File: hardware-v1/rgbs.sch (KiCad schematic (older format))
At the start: 10 parts, among them U15 NMEA_RGB, U2 SN74HCT245, U4 N2K_RGB, U5 WIFI_RGB

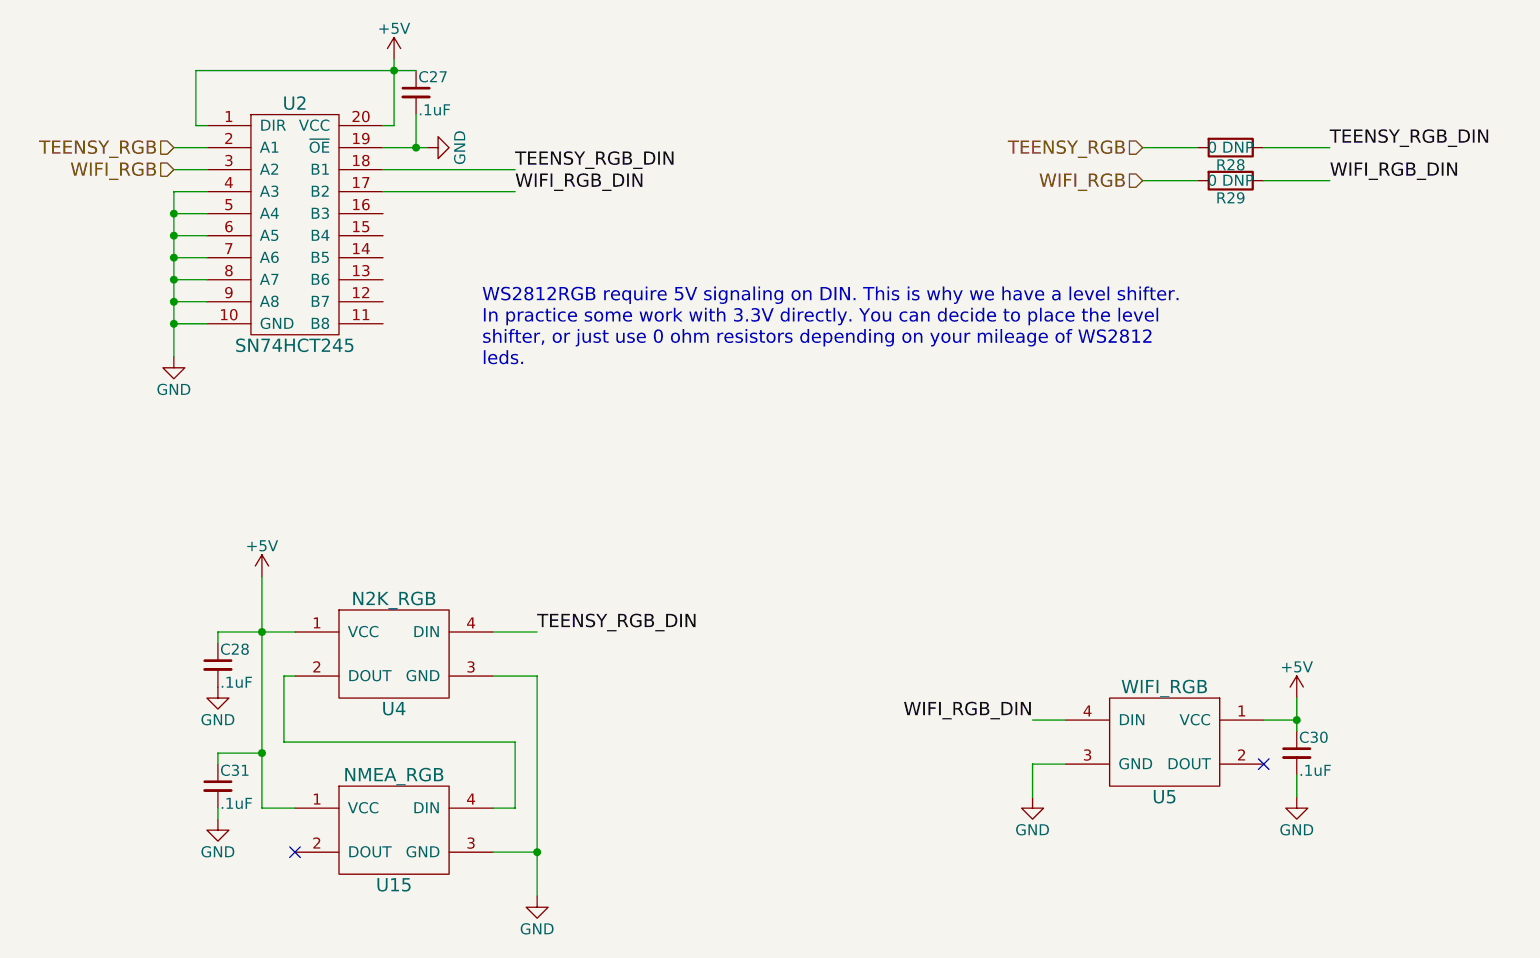
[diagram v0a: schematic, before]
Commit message: First draft of revision B
Lots of changes to the board. Almost completely re-layed out.

Will do some verification now.
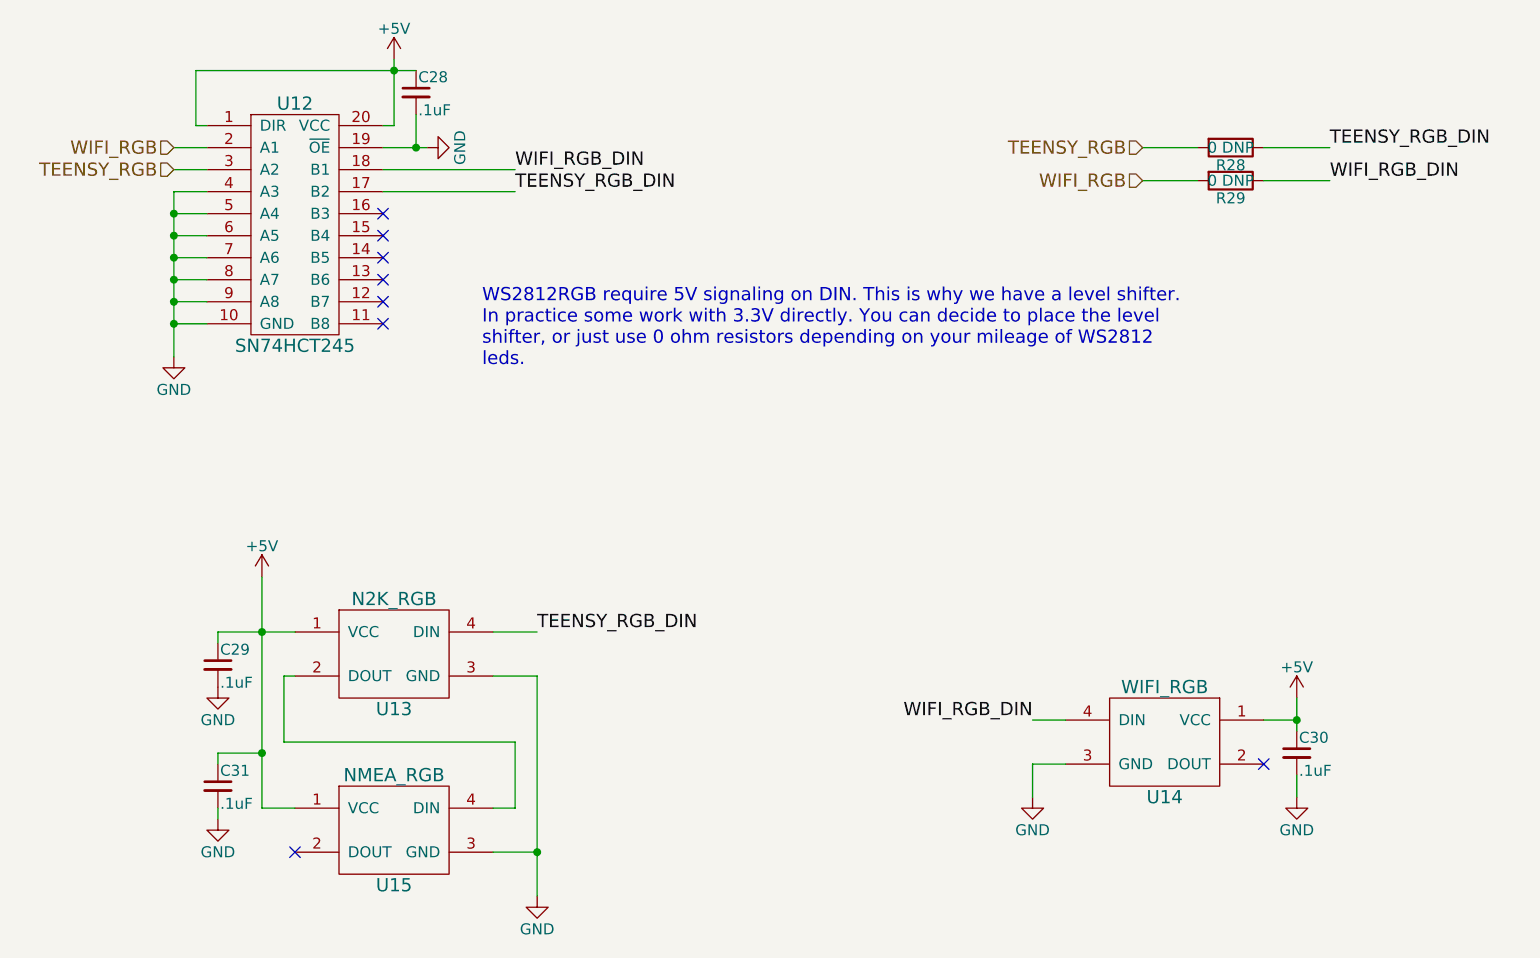
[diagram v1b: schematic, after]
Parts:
- renumbered C27 to C28, C28 to C29, U2 to U12, U4 to U13, U5 to U14
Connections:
- net TEENSY_RGB: now also U12.3 (A2); no longer U12.2 (A1)
- net TEENSY_RGB_DIN: now also U12.17 (B2); no longer U12.18 (B1)
- net WIFI_RGB: now also U12.2 (A1); no longer U12.3 (A2)
- net WIFI_RGB_DIN: now also U12.18 (B1); no longer U12.17 (B2)
- no-connect marks 2 -> 8
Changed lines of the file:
@@
 $EndDescr
 $Comp
-L WS2812RGB U4
+L WS2812RGB U13
 U 1 1 56A15737
 P 3750 4000
-F 0 "U4" H 3750 3750 60  0000 C CNN
+F 0 "U13" H 3750 3750 60  0000 C CNN
 F 1 "N2K_RGB" H 3750 4250 60  0000 C CNN
 F 2 "bb:WS2818RGB" H 3750 4050 60  0001 C CNN
@@
 $EndComp
 $Comp
-L GND #PWR073
+L GND #PWR074
 U 1 1 56A1574F
 P 4400 5100
-F 0 "#PWR073" H 4400 4850 50  0001 C CNN
+F 0 "#PWR074" H 4400 4850 50  0001 C CNN
 F 1 "GND" H 4400 4950 50  0000 C CNN
 F 2 "" H 4400 5100 60  0000 C CNN
@@
 $EndComp
 $Comp
-L +5V #PWR074
+L +5V #PWR075
 U 1 1 56A15759
 P 3150 3650
-F 0 "#PWR074" H 3150 3500 50  0001 C CNN
+F 0 "#PWR075" H 3150 3500 50  0001 C CNN
 F 1 "+5V" H 3150 3790 50  0000 C CNN
 F 2 "" H 3150 3650 60  0000 C CNN
@@
 NoConn ~ 3300 4900
 $Comp
-L C_Small C28
+L C_Small C29
 U 1 1 56A15760
 P 2950 4050
-F 0 "C28" H 2960 4120 50  0000 L CNN
+F 0 "C29" H 2960 4120 50  0000 L CNN
 F 1 ".1uF" H 2960 3970 50  0000 L CNN
 F 2 "Capacitors_SMD:C_0603" H 2950 4050 50  0001 C CNN
@@
 $EndComp
 $Comp
-L GND #PWR075
+L GND #PWR076
 U 1 1 56A15768
 P 2950 4150
-F 0 "#PWR075" H 2950 3900 50  0001 C CNN
+F 0 "#PWR076" H 2950 3900 50  0001 C CNN
 F 1 "GND" H 2950 4000 50  0000 C CNN
 F 2 "" H 2950 4150 60  0000 C CNN
@@
 $EndComp
 $Comp
-L GND #PWR076
+L GND #PWR077
 U 1 1 56A15779
 P 2950 4750
-F 0 "#PWR076" H 2950 4500 50  0001 C CNN
+F 0 "#PWR077" H 2950 4500 50  0001 C CNN
 F 1 "GND" H 2950 4600 50  0000 C CNN
 F 2 "" H 2950 4750 60  0000 C CNN
@@
 $EndComp
 $Comp
-L WS2812RGB U5
+L WS2812RGB U14
 U 1 1 56A16394
 P 7250 4400
-F 0 "U5" H 7250 4150 60  0000 C CNN
+F 0 "U14" H 7250 4150 60  0000 C CNN
 F 1 "WIFI_RGB" H 7250 4650 60  0000 C CNN
 F 2 "bb:WS2818RGB" H 7250 4450 60  0001 C CNN
@@
 $EndComp
 $Comp
-L GND #PWR077
+L GND #PWR078
 U 1 1 56A1639F
 P 6650 4650
-F 0 "#PWR077" H 6650 4400 50  0001 C CNN
+F 0 "#PWR078" H 6650 4400 50  0001 C CNN
 F 1 "GND" H 6650 4500 50  0000 C CNN
 F 2 "" H 6650 4650 60  0000 C CNN
@@
 $EndComp
 $Comp
-L +5V #PWR078
+L +5V #PWR079
 U 1 1 56A163A5
 P 7850 4200
-F 0 "#PWR078" H 7850 4050 50  0001 C CNN
+F 0 "#PWR079" H 7850 4050 50  0001 C CNN
 F 1 "+5V" H 7850 4340 50  0000 C CNN
 F 2 "" H 7850 4200 60  0000 C CNN
@@
 $EndComp
 $Comp
-L GND #PWR079
+L GND #PWR080
 U 1 1 56A163B7
 P 7850 4650
-F 0 "#PWR079" H 7850 4400 50  0001 C CNN
+F 0 "#PWR080" H 7850 4400 50  0001 C CNN
 F 1 "GND" H 7850 4500 50  0000 C CNN
 F 2 "" H 7850 4650 60  0000 C CNN
@@
 	1    0    0    -1
 $EndComp
+Text HLabel 2750 1700 0    60   Input ~ 0
+WIFI_RGB
 Text HLabel 2750 1800 0    60   Input ~ 0
-WIFI_RGB
-Text HLabel 2750 1700 0    60   Input ~ 0
 TEENSY_RGB
 $Comp
-L SN74HCT245 U2
+L SN74HCT245 U12
 U 1 1 56A1AACB
 P 3300 2050
-F 0 "U2" H 3300 2600 60  0000 C CNN
+F 0 "U12" H 3300 2600 60  0000 C CNN
 F 1 "SN74HCT245" H 3300 1500 60  0000 C CNN
 F 2 "Housings_SSOP:TSSOP-20_4.4x6.5mm_Pitch0.65mm" H 3250 2000 60  0001 C CNN
@@
 $EndComp
 $Comp
-L +5V #PWR080
+L +5V #PWR081
 U 1 1 56A1B099
 P 3750 1300
-F 0 "#PWR080" H 3750 1150 50  0001 C CNN
+F 0 "#PWR081" H 3750 1150 50  0001 C CNN
 F 1 "+5V" H 3750 1440 50  0000 C CNN
 F 2 "" H 3750 1300 60  0000 C CNN
@@
 $EndComp
 $Comp
-L GND #PWR081
+L GND #PWR082
 U 1 1 56A1B102
 P 2750 2650
-F 0 "#PWR081" H 2750 2400 50  0001 C CNN
+F 0 "#PWR082" H 2750 2400 50  0001 C CNN
 F 1 "GND" H 2750 2500 50  0000 C CNN
 F 2 "" H 2750 2650 60  0000 C CNN
@@
 	3700 1700 3900 1700
 $Comp
-L GND #PWR082
+L GND #PWR083
 U 1 1 56A1B2CF
 P 3900 1700
-F 0 "#PWR082" H 3900 1450 50  0001 C CNN
+F 0 "#PWR083" H 3900 1450 50  0001 C CNN
 F 1 "GND" H 3900 1550 50  0000 C CNN
 F 2 "" H 3900 1700 60  0000 C CNN
@@
 Wire Wire Line
 	3700 1900 4300 1900
+Text Label 4300 1900 0    60   ~ 0
+TEENSY_RGB_DIN
 Text Label 4300 1800 0    60   ~ 0
-TEENSY_RGB_DIN
-Text Label 4300 1900 0    60   ~ 0
 WIFI_RGB_DIN
 Text HLabel 7150 1700 0    60   Input ~ 0
@@
 WS2812RGB require 5V signaling on DIN. This is why we have a level shifter.\nIn practice some work with 3.3V directly. You can decide to place the level\nshifter, or just use 0 ohm resistors depending on your mileage of WS2812\nleds.
 $Comp
-L C_Small C27
+L C_Small C28
 U 1 1 56A1CB34
 P 3850 1450
-F 0 "C27" H 3860 1520 50  0000 L CNN
+F 0 "C28" H 3860 1520 50  0000 L CNN
 F 1 ".1uF" H 3860 1370 50  0000 L CNN
 F 2 "Capacitors_SMD:C_0603" H 3850 1450 50  0001 C CNN
@@
 	3850 1700 3850 1550
 Connection ~ 3850 1700
+NoConn ~ 3700 2000
+NoConn ~ 3700 2100
+NoConn ~ 3700 2200
+NoConn ~ 3700 2300
+NoConn ~ 3700 2400
+NoConn ~ 3700 2500
 $EndSCHEMATC

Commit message: Finalizing revB
 - Added part numbers on all parts (in kicad PartNumber field)
 - Some finicking in a bunch of corners
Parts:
- C28, C29, C30, C31: PartNumber (none) -> CC0603KPX7R7BB104
- U12: PartNumber (none) -> SN74HCT245PWR
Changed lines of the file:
@@
 F 2 "Capacitors_SMD:C_0603" H 2950 4050 50  0001 C CNN
 F 3 "" H 2950 4050 50  0000 C CNN
+F 4 "CC0603KPX7R7BB104" H 2950 4050 60  0001 C CNN "PartNumber"
 	1    2950 4050
 	1    0    0    -1
@@
 F 2 "Capacitors_SMD:C_0603" H 2950 4600 50  0001 C CNN
 F 3 "" H 2950 4600 50  0000 C CNN
+F 4 "CC0603KPX7R7BB104" H 2950 4600 60  0001 C CNN "PartNumber"
 	1    2950 4600
 	1    0    0    -1
@@
 F 2 "Capacitors_SMD:C_0603" H 7850 4450 50  0001 C CNN
 F 3 "" H 7850 4450 50  0000 C CNN
+F 4 "CC0603KPX7R7BB104" H 7850 4450 60  0001 C CNN "PartNumber"
 	1    7850 4450
 	1    0    0    -1
@@
 F 2 "Housings_SSOP:TSSOP-20_4.4x6.5mm_Pitch0.65mm" H 3250 2000 60  0001 C CNN
 F 3 "" H 3250 2000 60  0000 C CNN
+F 4 "SN74HCT245PWR" H 3300 2050 60  0001 C CNN "PartNumber"
 	1    3300 2050
 	1    0    0    -1
@@
 F 2 "Capacitors_SMD:C_0603" H 3850 1450 50  0001 C CNN
 F 3 "" H 3850 1450 50  0000 C CNN
+F 4 "CC0603KPX7R7BB104" H 3850 1450 60  0001 C CNN "PartNumber"
 	1    3850 1450
 	1    0    0    -1

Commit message: Final touches + v1revb sent to oshpark
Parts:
- renumbered C28 to C27, C29 to C28, C30 to C29, C31 to C30
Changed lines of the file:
@@
 $EndComp
 $Comp
-L GND #PWR074
+L GND #PWR073
 U 1 1 56A1574F
 P 4400 5100
-F 0 "#PWR074" H 4400 4850 50  0001 C CNN
+F 0 "#PWR073" H 4400 4850 50  0001 C CNN
 F 1 "GND" H 4400 4950 50  0000 C CNN
 F 2 "" H 4400 5100 60  0000 C CNN
@@
 $EndComp
 $Comp
-L +5V #PWR075
+L +5V #PWR074
 U 1 1 56A15759
 P 3150 3650
-F 0 "#PWR075" H 3150 3500 50  0001 C CNN
+F 0 "#PWR074" H 3150 3500 50  0001 C CNN
 F 1 "+5V" H 3150 3790 50  0000 C CNN
 F 2 "" H 3150 3650 60  0000 C CNN
@@
 NoConn ~ 3300 4900
 $Comp
-L C_Small C29
+L C_Small C28
 U 1 1 56A15760
 P 2950 4050
-F 0 "C29" H 2960 4120 50  0000 L CNN
+F 0 "C28" H 2960 4120 50  0000 L CNN
 F 1 ".1uF" H 2960 3970 50  0000 L CNN
 F 2 "Capacitors_SMD:C_0603" H 2950 4050 50  0001 C CNN
@@
 $EndComp
 $Comp
-L GND #PWR076
+L GND #PWR075
 U 1 1 56A15768
 P 2950 4150
-F 0 "#PWR076" H 2950 3900 50  0001 C CNN
+F 0 "#PWR075" H 2950 3900 50  0001 C CNN
 F 1 "GND" H 2950 4000 50  0000 C CNN
 F 2 "" H 2950 4150 60  0000 C CNN
@@
 $EndComp
 $Comp
-L C_Small C31
+L C_Small C30
 U 1 1 56A1576E
 P 2950 4600
-F 0 "C31" H 2960 4670 50  0000 L CNN
+F 0 "C30" H 2960 4670 50  0000 L CNN
 F 1 ".1uF" H 2960 4520 50  0000 L CNN
 F 2 "Capacitors_SMD:C_0603" H 2950 4600 50  0001 C CNN
@@
 $EndComp
 $Comp
-L GND #PWR077
+L GND #PWR076
 U 1 1 56A15779
 P 2950 4750
-F 0 "#PWR077" H 2950 4500 50  0001 C CNN
+F 0 "#PWR076" H 2950 4500 50  0001 C CNN
 F 1 "GND" H 2950 4600 50  0000 C CNN
 F 2 "" H 2950 4750 60  0000 C CNN
@@
 $EndComp
 $Comp
-L GND #PWR078
+L GND #PWR077
 U 1 1 56A1639F
 P 6650 4650
-F 0 "#PWR078" H 6650 4400 50  0001 C CNN
+F 0 "#PWR077" H 6650 4400 50  0001 C CNN
 F 1 "GND" H 6650 4500 50  0000 C CNN
 F 2 "" H 6650 4650 60  0000 C CNN
@@
 $EndComp
 $Comp
-L +5V #PWR079
+L +5V #PWR078
 U 1 1 56A163A5
 P 7850 4200
-F 0 "#PWR079" H 7850 4050 50  0001 C CNN
+F 0 "#PWR078" H 7850 4050 50  0001 C CNN
 F 1 "+5V" H 7850 4340 50  0000 C CNN
 F 2 "" H 7850 4200 60  0000 C CNN
@@
 NoConn ~ 7700 4500
 $Comp
-L C_Small C30
+L C_Small C29
 U 1 1 56A163AE
 P 7850 4450
-F 0 "C30" H 7860 4520 50  0000 L CNN
+F 0 "C29" H 7860 4520 50  0000 L CNN
 F 1 ".1uF" H 7860 4370 50  0000 L CNN
 F 2 "Capacitors_SMD:C_0603" H 7850 4450 50  0001 C CNN
@@
 $EndComp
 $Comp
-L GND #PWR080
+L GND #PWR079
 U 1 1 56A163B7
 P 7850 4650
-F 0 "#PWR080" H 7850 4400 50  0001 C CNN
+F 0 "#PWR079" H 7850 4400 50  0001 C CNN
 F 1 "GND" H 7850 4500 50  0000 C CNN
 F 2 "" H 7850 4650 60  0000 C CNN
@@
 $EndComp
 $Comp
-L +5V #PWR081
+L +5V #PWR080
 U 1 1 56A1B099
 P 3750 1300
-F 0 "#PWR081" H 3750 1150 50  0001 C CNN
+F 0 "#PWR080" H 3750 1150 50  0001 C CNN
 F 1 "+5V" H 3750 1440 50  0000 C CNN
 F 2 "" H 3750 1300 60  0000 C CNN
@@
 $EndComp
 $Comp
-L GND #PWR082
+L GND #PWR081
 U 1 1 56A1B102
 P 2750 2650
-F 0 "#PWR082" H 2750 2400 50  0001 C CNN
+F 0 "#PWR081" H 2750 2400 50  0001 C CNN
 F 1 "GND" H 2750 2500 50  0000 C CNN
 F 2 "" H 2750 2650 60  0000 C CNN
@@
 	3700 1700 3900 1700
 $Comp
-L GND #PWR083
+L GND #PWR082
 U 1 1 56A1B2CF
 P 3900 1700
-F 0 "#PWR083" H 3900 1450 50  0001 C CNN
+F 0 "#PWR082" H 3900 1450 50  0001 C CNN
 F 1 "GND" H 3900 1550 50  0000 C CNN
 F 2 "" H 3900 1700 60  0000 C CNN
@@
 WS2812RGB require 5V signaling on DIN. This is why we have a level shifter.\nIn practice some work with 3.3V directly. You can decide to place the level\nshifter, or just use 0 ohm resistors depending on your mileage of WS2812\nleds.
 $Comp
-L C_Small C28
+L C_Small C27
 U 1 1 56A1CB34
 P 3850 1450
-F 0 "C28" H 3860 1520 50  0000 L CNN
+F 0 "C27" H 3860 1520 50  0000 L CNN
 F 1 ".1uF" H 3860 1370 50  0000 L CNN
 F 2 "Capacitors_SMD:C_0603" H 3850 1450 50  0001 C CNN
